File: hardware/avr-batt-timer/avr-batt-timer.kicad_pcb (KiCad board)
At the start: 2 copper layers, 24.1 x 49.9 mm, 13 parts, among them J1 XT60PW-M, J2 XT60PW-F, J3 Conn_01x05_Pin, U1 ATtiny5, U2 L78L05_SOT89

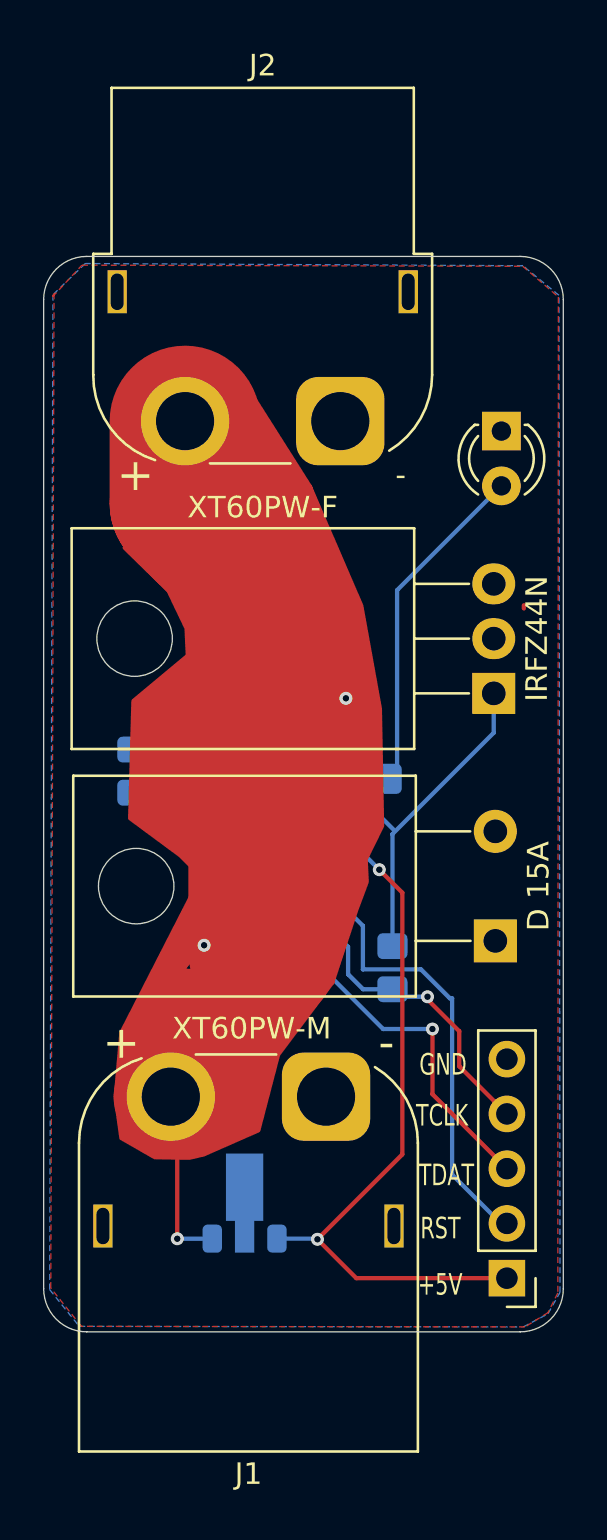
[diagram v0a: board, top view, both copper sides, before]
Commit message: Fixed TPICLK pin connection. Replaced programming pins with holes.
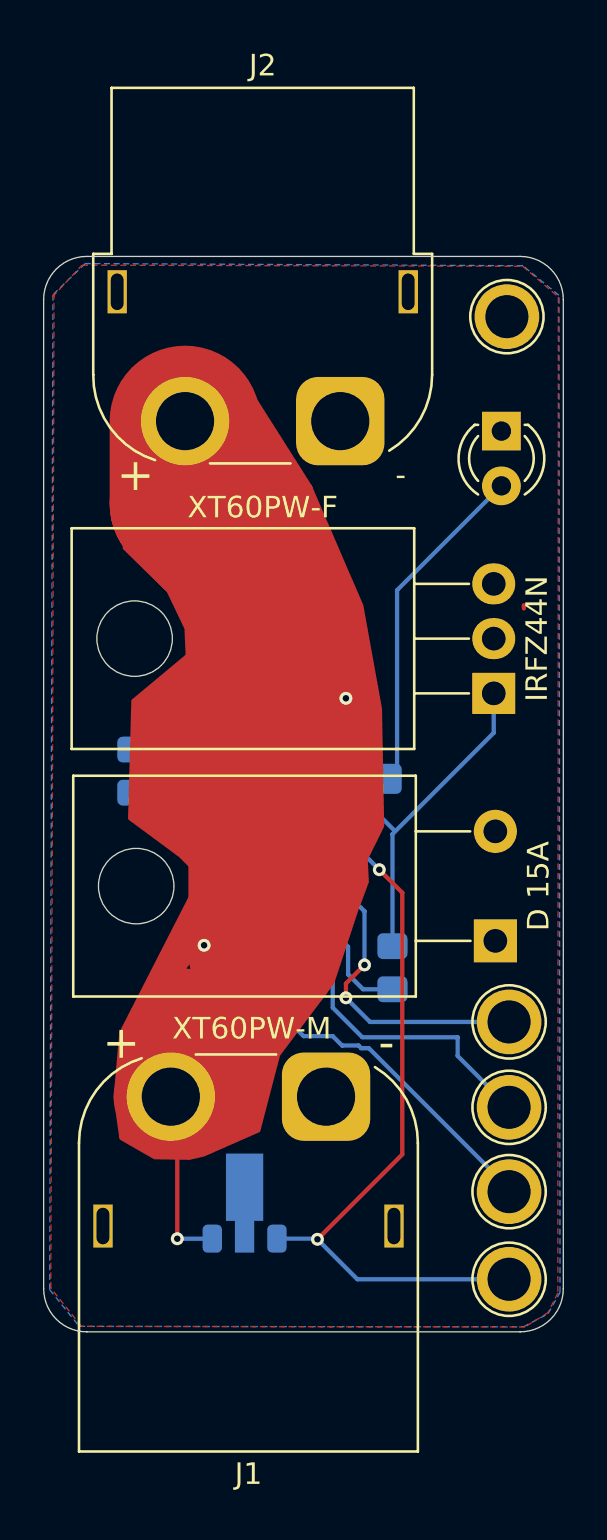
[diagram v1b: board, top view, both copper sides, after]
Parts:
- removed J3: Conn_01x05_Pin, Connector_PinHeader_2.54mm:PinHeader_1x05_P2.54mm_Vertical
- added TP1: +5V, TestPoint:TestPoint_Plated_Hole_D2.0mm, F.Cu at (153.8, 106.1)
- added TP2: RST, TestPoint:TestPoint_Plated_Hole_D2.0mm, F.Cu at (153.8, 94.2)
- added TP3: TDAT, TestPoint:TestPoint_Plated_Hole_D2.0mm, F.Cu at (153.8, 98.1)
- added TP4: TCLK, TestPoint:TestPoint_Plated_Hole_D2.0mm, F.Cu at (153.8, 102.1)
- added TP5: GND, TestPoint:TestPoint_Plated_Hole_D2.0mm, F.Cu at (153.7, 61.5)
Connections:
- R1 pad 2: VSENSE -> TPICLK
- R2 pad 1: VSENSE -> TPICLK
- R3 pad 2: TPICLK -> Net-(U1-PB2)
- U1 pad 3: VSENSE -> TPICLK
- U1 pad 4: TPICLK -> Net-(U1-PB2)
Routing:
- net Net-(U1-PB2): track 0.00 -> 10.3 mm
- net RESET: track 21.8 -> 15.9 mm, vias 0 -> 2
- net VSENSE: track 5.09 -> 0.00 mm
- net TPICLK: track 18.6 -> 20.5 mm, vias 1 -> 0
- net TPIDATA: track 16.4 -> 14.8 mm, vias 1 -> 0
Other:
- board text removed: "+5V"
- board text removed: "GND"
- board text removed: "RST"
- board text removed: "TCLK"
- board text removed: "TDAT"

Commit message: Last version with attiny5.
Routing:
- net GND: track 3.46 -> 8.63 mm, vias 0 -> 1
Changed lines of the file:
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@@
 		(property "Value" "+5V"
 			(at -2.9972 0.0508 0)
-			(layer "F.Fab")
+			(layer "F.SilkS")
 			(effects
 				(font
@@
 		(property "Value" "RST"
 			(at -2.8956 0.254 0)
-			(layer "F.Fab")
+			(layer "F.SilkS")
 			(effects
 				(font
@@
 		(property "Value" "TDAT"
 			(at -3.048 0.1016 0)
-			(layer "F.Fab")
+			(layer "F.SilkS")
 			(effects
 				(font
@@
 		(property "Value" "TCLK"
 			(at -3.1496 0.3556 0)
-			(layer "F.Fab")
+			(layer "F.SilkS")
 			(effects
 				(font
@@
 		(property "Value" "GND"
 			(at 0 2.45 0)
-			(layer "F.Fab")
+			(layer "F.SilkS")
 			(effects
 				(font
@@
 	)
 	(segment
+		(start 145.1864 97.5048)
+		(end 145.332 97.6504)
+		(width 0.2)
+		(layer "F.Cu")
+		(net 3)
+	)
+	(segment
+		(start 145.1864 94.1324)
+		(end 145.1864 97.5048)
+		(width 0.2)
+		(layer "F.Cu")
+		(net 3)
+	)
+	(via
+		(at 145.1864 94.1324)
+		(size 0.6)
+		(drill 0.3)
+		(layers "F.Cu" "B.Cu")
+		(net 3)
+	)
+	(segment
+		(start 144.3322 92.8878)
+		(end 144.3322 93.2782)
+		(width 0.2)
+		(layer "B.Cu")
+		(net 3)
+	)
+	(segment
+		(start 144.3322 93.2782)
+		(end 145.1864 94.1324)
+		(width 0.2)
+		(layer "B.Cu")
+		(net 3)
+	)
+	(segment
